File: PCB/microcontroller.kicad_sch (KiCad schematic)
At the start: 0 parts

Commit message: Further major components
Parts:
- added J1: Micro_SD_Card, Connector_Card:microSD_HC_Molex_47219-2001, symbol Connector:Micro_SD_Card
- added U2: STM32F401RETx, Package_QFP:LQFP-64_10x10mm_P0.5mm, symbol MCU_ST_STM32F4:STM32F401RETx
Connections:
- new net: U2.18 (VSS), U2.31 (VSS), U2.47 (VSS), U2.63 (VSS)
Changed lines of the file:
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@@
 (kicad_sch (version 20230121) (generator eeschema)
   (paper "A4")
+  (symbol (lib_id "Connector:Micro_SD_Card") (at 158.75 49.53 0) (unit 1)
+    (in_bom yes) (on_board yes) (dnp no) (fields_autoplaced)
+    (property "Reference" "J1" (at 159.385 31.75 0)
+      (effects (font (size 1.27 1.27)))
+    )
+    (property "Value" "Micro_SD_Card" (at 159.385 34.29 0)
+      (effects (font (size 1.27 1.27)))
+    )
+    (property "Footprint" "Connector_Card:microSD_HC_Molex_47219-2001" (at 187.96 41.91 0)
+      (effects (font (size 1.27 1.27)) hide)
+    )
+    (property "Datasheet" "http://katalog.we-online.de/em/datasheet/693072010801.pdf" (at 158.75 49.53 0)
+      (effects (font (size 1.27 1.27)) hide)
+    )
+    (pin "1")
+    (pin "2")
+    (pin "3")
+    (pin "4")
+    (pin "5")
+    (pin "6")
+    (pin "7")
+    (pin "8")
+    (pin "9")
+    (instances
+      (project "motor_tracker"
+        (path "/a8928dcf-7fea-46f0-8c15-a3fa49b43e6b/0c29d405-cd4c-45ef-9d08-777d8a682a5c"
+          (reference "J1") (unit 1)
+        )
+      )
+    )
+  )
+  (symbol (lib_id "MCU_ST_STM32F4:STM32F401RETx") (at 77.47 80.01 0) (unit 1)
+    (in_bom yes) (on_board yes) (dnp no) (fields_autoplaced)
+    (property "Reference" "U2" (at 81.9659 125.73 0)
+      (effects (font (size 1.27 1.27)) (justify left))
+    )
+    (property "Value" "STM32F401RETx" (at 81.9659 128.27 0)
+      (effects (font (size 1.27 1.27)) (justify left))
+    )
+    (property "Footprint" "Package_QFP:LQFP-64_10x10mm_P0.5mm" (at 64.77 123.19 0)
+      (effects (font (size 1.27 1.27)) (justify right) hide)
+    )
+    (property "Datasheet" "https://www.st.com/resource/en/datasheet/stm32f401re.pdf" (at 77.47 80.01 0)
+      (effects (font (size 1.27 1.27)) hide)
+    )
+    (pin "1")
+    (pin "10")
+    (pin "11")
+    (pin "12")
+    (pin "13")
+    (pin "14")
+    (pin "15")
+    (pin "16")
+    (pin "17")
+    (pin "18")
+    (pin "19")
+    (pin "2")
+    (pin "20")
+    (pin "21")
+    (pin "22")
+    (pin "23")
+    (pin "24")
+    (pin "25")
+    (pin "26")
+    (pin "27")
+    (pin "28")
+    (pin "29")
+    (pin "3")
+    (pin "30")
+    (pin "31")
+    (pin "32")
+    (pin "33")
+    (pin "34")
+    (pin "35")
+    (pin "36")
+    (pin "37")
+    (pin "38")
+    (pin "39")
+    (pin "4")
+    (pin "40")
+    (pin "41")
+    (pin "42")
+    (pin "43")
+    (pin "44")
+    (pin "45")
+    (pin "46")
+    (pin "47")
+    (pin "48")
+    (pin "49")
+    (pin "5")
+    (pin "50")
+    (pin "51")
+    (pin "52")
+    (pin "53")
+    (pin "54")
+    (pin "55")
+    (pin "56")
+    (pin "57")
+    (pin "58")
+    (pin "59")
+    (pin "6")
+    (pin "60")
+    (pin "61")
+    (pin "62")
+    (pin "63")
+    (pin "64")
+    (pin "7")
+    (pin "8")
+    (pin "9")
+    (instances
+      (project "motor_tracker"
+        (path "/a8928dcf-7fea-46f0-8c15-a3fa49b43e6b/0c29d405-cd4c-45ef-9d08-777d8a682a5c"
+          (reference "U2") (unit 1)
+        )
+      )
+    )
+  )
 )

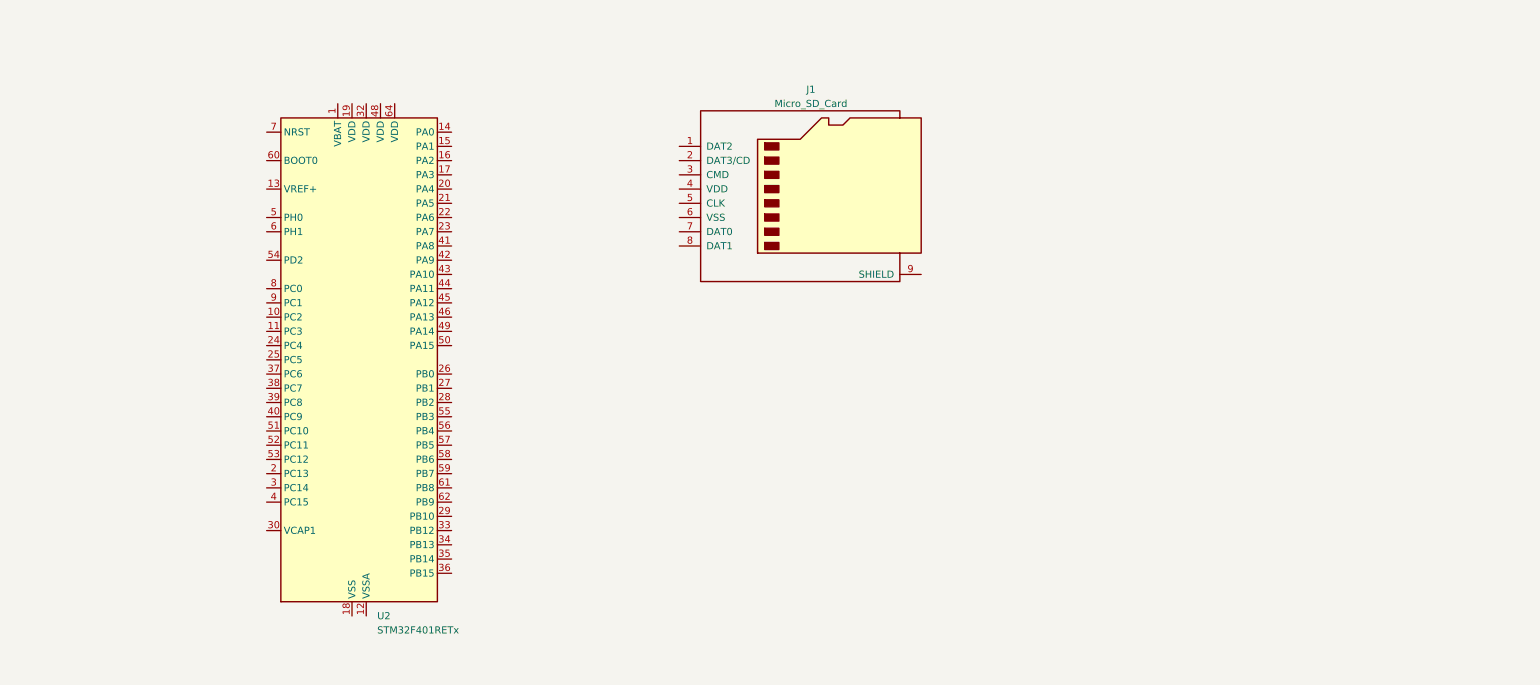
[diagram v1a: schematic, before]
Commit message: Added basic componenets to uC
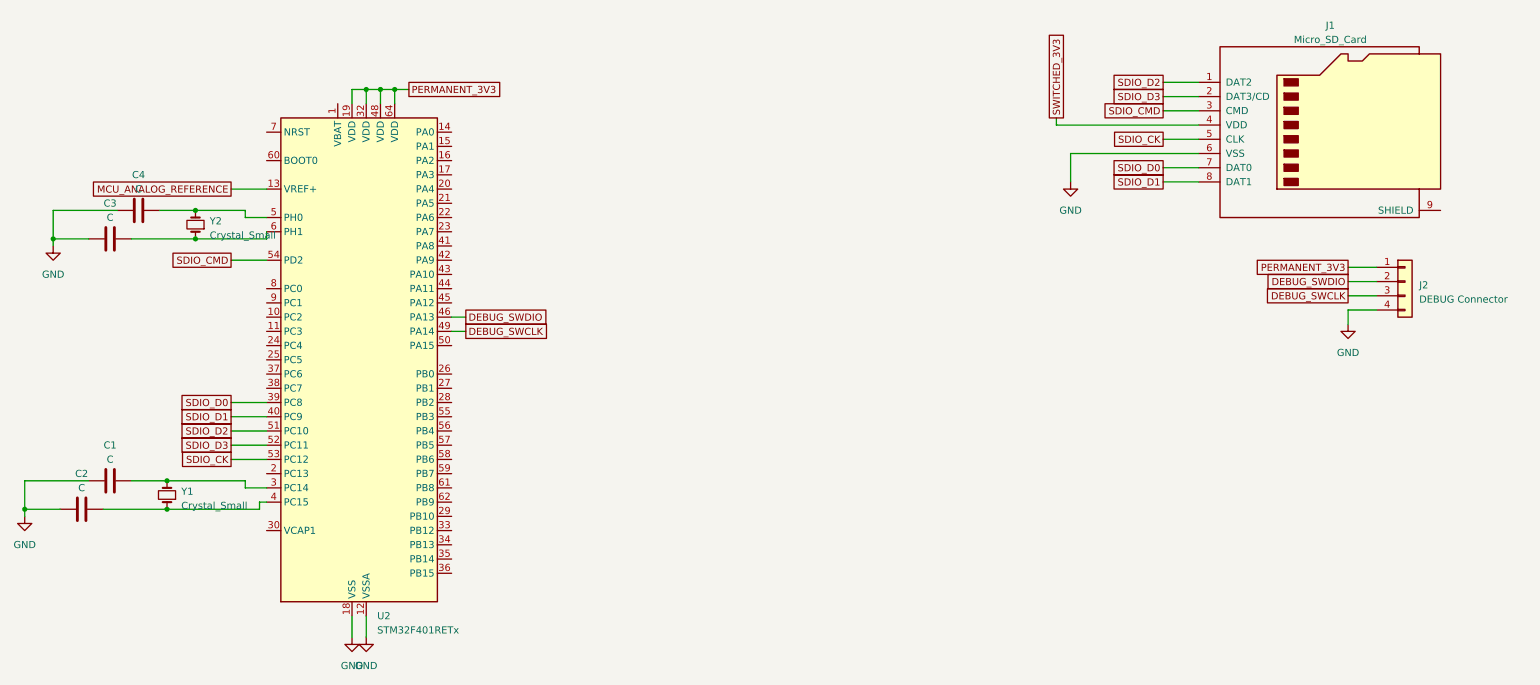
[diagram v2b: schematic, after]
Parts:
- added C1, C2, C3, C4: C, Capacitor_SMD:C_0201_0603Metric_Pad0.64x0.40mm_HandSolder, symbol Device:C
- added J2: DEBUG Connector, Connector_PinHeader_2.54mm:PinHeader_1x04_P2.54mm_Vertical, symbol Connector_Generic:Conn_01x04
- added Y1: Crystal_Small, Crystal:Crystal_SMD_5032-4Pin_5.0x3.2mm, symbol Device:Crystal_Small
- added Y2: Crystal_Small, Crystal:Crystal_C38-LF_D3.0mm_L8.0mm_Horizontal_1EP_style1, symbol Device:Crystal_Small
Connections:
- net SDIO_D2: now reaches J1.1 (DAT2)
- net SDIO_D2: now also U2.51 (PC10)
- net SDIO_D3: now reaches J1.2 (DAT3/CD)
- net SDIO_D3: now also U2.52 (PC11)
- net SDIO_CMD: now reaches J1.3 (CMD)
- net SDIO_CMD: now also U2.54 (PD2)
- net SWITCHED_3V3: now reaches J1.4 (VDD)
- net SDIO_CK: now reaches J1.5 (CLK)
- net SDIO_CK: now also U2.53 (PC12)
- net GND: now reaches J1.6 (VSS)
- net GND: now also U2.12 (VSSA), U2.18 (VSS), U2.31 (VSS), U2.47 (VSS), U2.63 (VSS), C1.2, C2.2, C3.2, C4.2, J2.4 (Pin_4)
- net SDIO_D0: now reaches J1.7 (DAT0)
- net SDIO_D0: now also U2.39 (PC8)
- net SDIO_D1: now reaches J1.8 (DAT1)
- net SDIO_D1: now also U2.40 (PC9)
- net MCU_ANALOG_REFERENCE: now reaches U2.13 (VREF+)
- net PERMANENT_3V3: now reaches U2.19 (VDD)
- net PERMANENT_3V3: now also U2.32 (VDD), U2.48 (VDD), U2.64 (VDD), J2.1 (Pin_1)
- net at U2.3 (PC14): now also C1.1, Y1.2
- net at U2.4 (PC15): now also C2.1, Y1.1
- net DEBUG_SWDIO: now reaches U2.46 (PA13)
- net DEBUG_SWDIO: now also J2.2 (Pin_2)
- net DEBUG_SWCLK: now reaches U2.49 (PA14)
- net DEBUG_SWCLK: now also J2.3 (Pin_3)
- net at U2.5 (PH0): now also C4.1, Y2.2
- net at U2.6 (PH1): now also C3.1, Y2.1
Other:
- moved on the sheet: J1

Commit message: Added USB connector
Added acceleration sensor

Added combined gyro and acceleration sensor
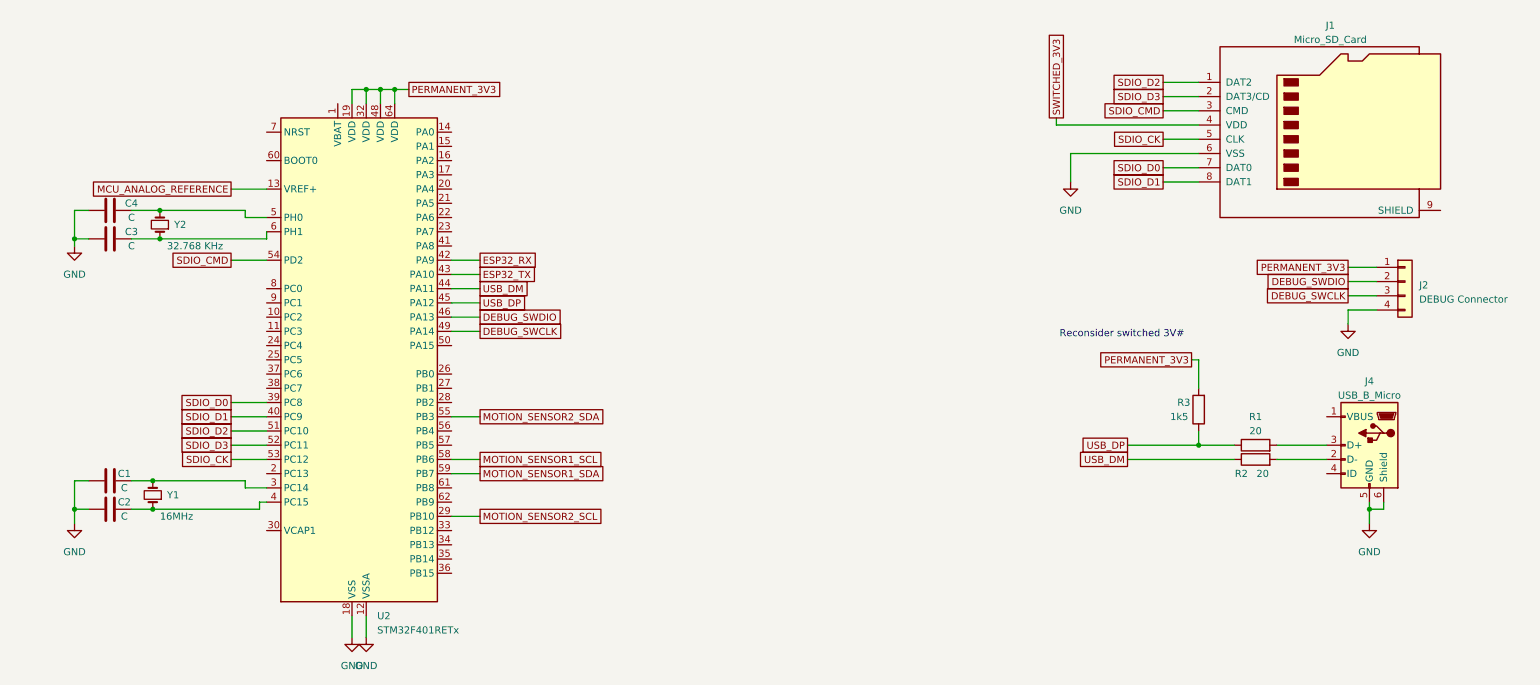
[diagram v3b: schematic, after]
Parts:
- added J4: USB_B_Micro, Connector_USB:USB_Micro-B_Molex-105017-0001, symbol Connector:USB_B_Micro
- added R1, R2: 20, Resistor_SMD:R_0603_1608Metric_Pad0.98x0.95mm_HandSolder, symbol Device:R
- added R3: 1k5, Resistor_SMD:R_0603_1608Metric_Pad0.98x0.95mm_HandSolder, symbol Device:R
- J1: Hestore (none) -> https://www.hestore.hu/prod_10035282.html
- Y1: value Crystal_Small -> 16MHz
- Y2: value Crystal_Small -> 32.768 KHz
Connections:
- net GND: now also J4.5 (GND), J4.6 (Shield)
- net PERMANENT_3V3: now also R3.2
- net MOTION_SENSOR2_SCL: now reaches U2.29 (PB10)
- net ESP32_RX: now reaches U2.42 (PA9)
- net ESP32_TX: now reaches U2.43 (PA10)
- net USB_DM: now reaches U2.44 (PA11)
- net USB_DM: now also R2.1
- net USB_DP: now reaches U2.45 (PA12)
- net USB_DP: now also R1.1, R3.1
- net MOTION_SENSOR2_SDA: now reaches U2.55 (PB3)
- net MOTION_SENSOR1_SCL: now reaches U2.58 (PB6)
- net MOTION_SENSOR1_SDA: now reaches U2.59 (PB7)
- new net: J4.2 (D-), R2.2
- new net: J4.3 (D+), R1.2
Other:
- note added: "Reconsider switched 3V#"
- moved on the sheet: C2, C4, Y1, Y2

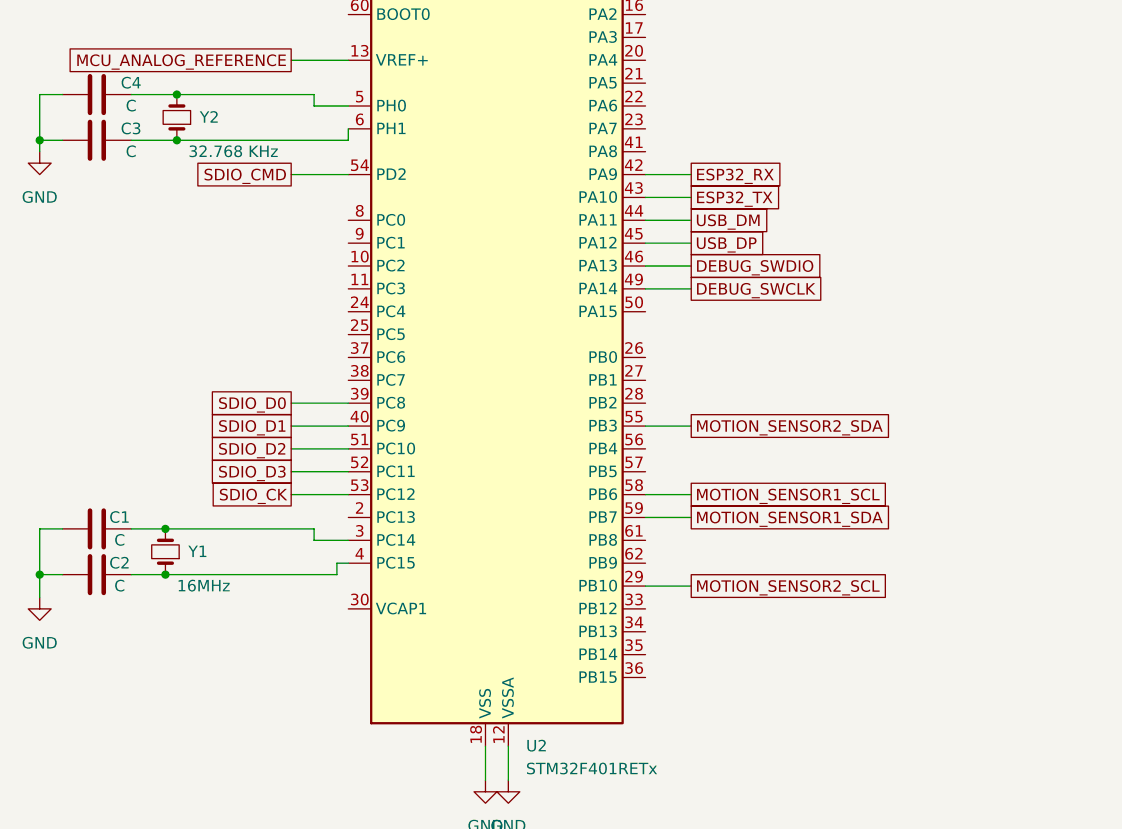
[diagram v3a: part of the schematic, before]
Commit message: Added connector for GPS
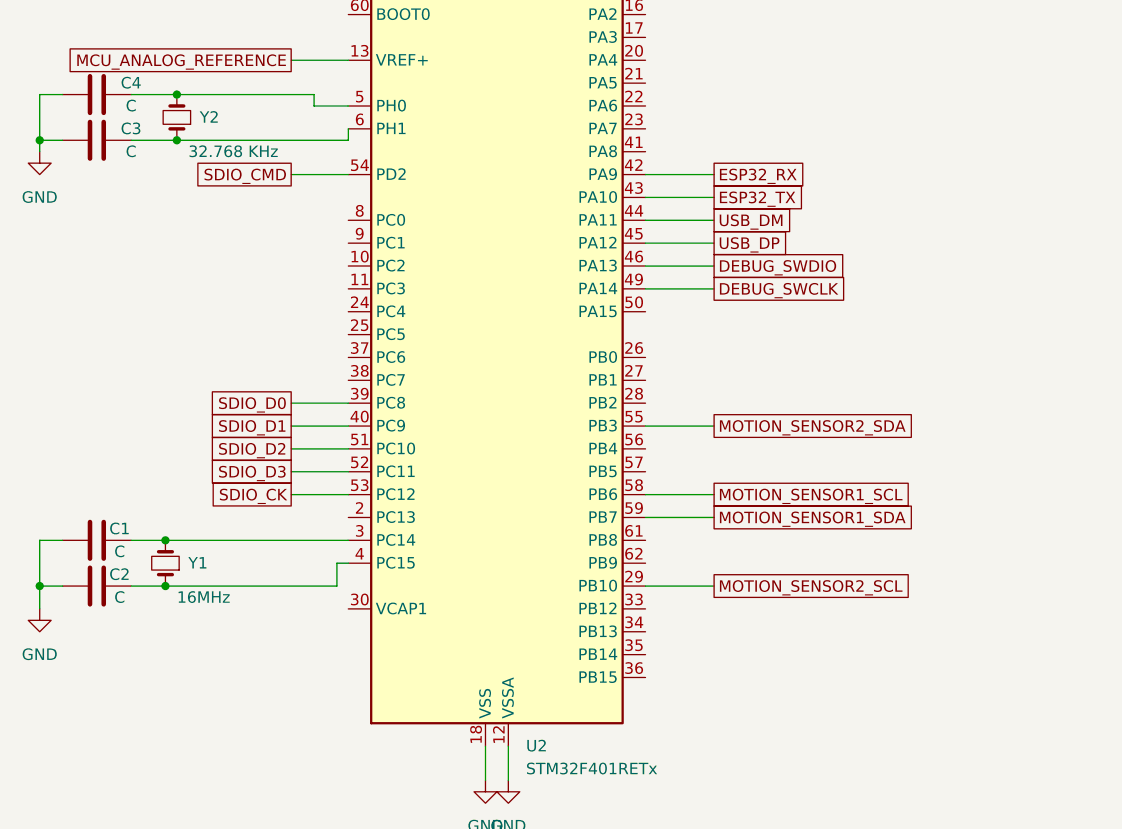
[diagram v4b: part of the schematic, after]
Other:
- moved on the sheet: C1, C2, Y1

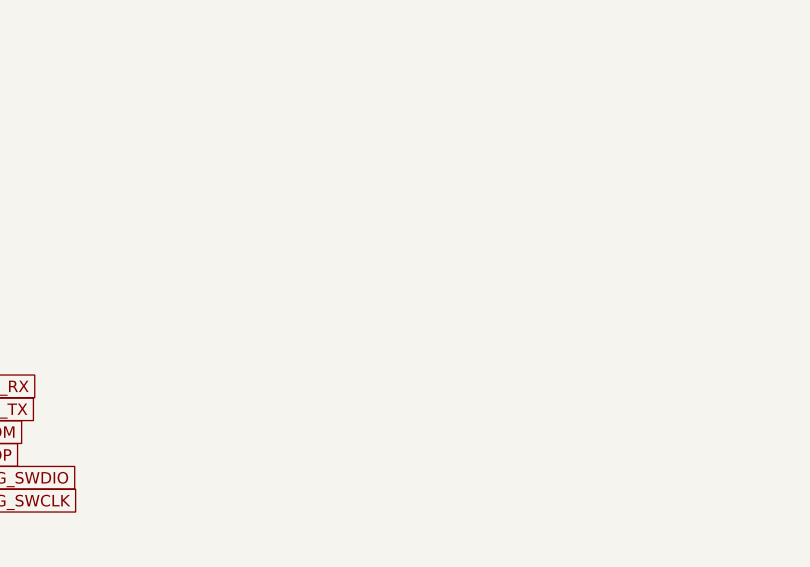
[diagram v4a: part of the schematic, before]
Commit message: Polarity protection in Power Management
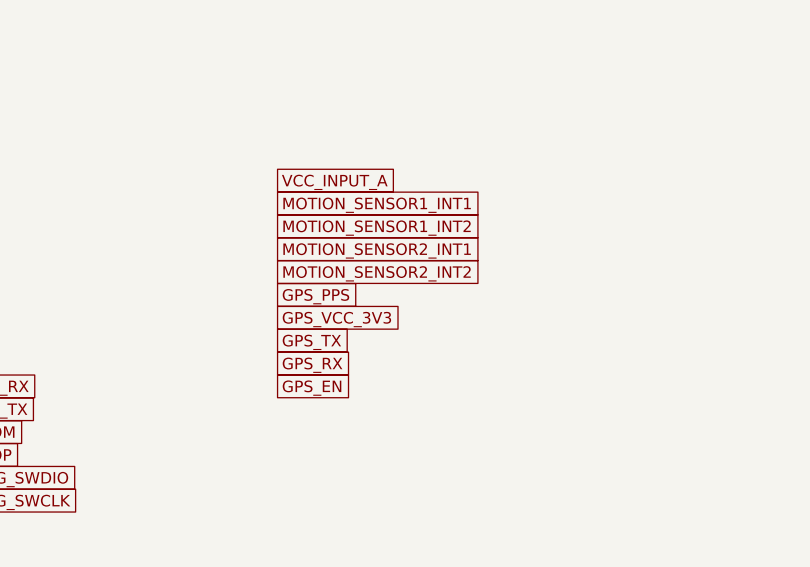
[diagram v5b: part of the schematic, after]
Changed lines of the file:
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@@
     (effects (font (size 1.27 1.27)) (justify right bottom))
   )
+  (global_label "MOTION_SENSOR1_INT1" (shape passive) (at 139.7 41.91 0) (fields_autoplaced)
+    (effects (font (size 1.27 1.27)) (justify left))
+    (property "Intersheetrefs" "${INTERSHEET_REFS}" (at 163.2659 41.91 0)
+      (effects (font (size 1.27 1.27)) (justify left) hide)
+    )
+  )
   (global_label "SDIO_D1" (shape passive) (at 222.25 48.26 180) (fields_autoplaced)
     (effects (font (size 1.27 1.27)) (justify right))
@@
     )
   )
+  (global_label "MOTION_SENSOR2_INT1" (shape passive) (at 139.7 46.99 0) (fields_autoplaced)
+    (effects (font (size 1.27 1.27)) (justify left))
+    (property "Intersheetrefs" "${INTERSHEET_REFS}" (at 163.2659 46.99 0)
+      (effects (font (size 1.27 1.27)) (justify left) hide)
+    )
+  )
+  (global_label "GPS_EN" (shape passive) (at 139.7 62.23 0) (fields_autoplaced)
+    (effects (font (size 1.27 1.27)) (justify left))
+    (property "Intersheetrefs" "${INTERSHEET_REFS}" (at 148.6911 62.23 0)
+      (effects (font (size 1.27 1.27)) (justify left) hide)
+    )
+  )
   (global_label "SDIO_CMD" (shape passive) (at 222.25 35.56 180) (fields_autoplaced)
     (effects (font (size 1.27 1.27)) (justify right))
@@
     )
   )
+  (global_label "VCC_INPUT_A" (shape passive) (at 139.7 39.37 0) (fields_autoplaced)
+    (effects (font (size 1.27 1.27)) (justify left))
+    (property "Intersheetrefs" "${INTERSHEET_REFS}" (at 153.6503 39.37 0)
+      (effects (font (size 1.27 1.27)) (justify left) hide)
+    )
+  )
+  (global_label "GPS_VCC_3V3" (shape passive) (at 139.7 54.61 0) (fields_autoplaced)
+    (effects (font (size 1.27 1.27)) (justify left))
+    (property "Intersheetrefs" "${INTERSHEET_REFS}" (at 154.3154 54.61 0)
+      (effects (font (size 1.27 1.27)) (justify left) hide)
+    )
+  )
+  (global_label "GPS_TX" (shape passive) (at 139.7 57.15 0) (fields_autoplaced)
+    (effects (font (size 1.27 1.27)) (justify left))
+    (property "Intersheetrefs" "${INTERSHEET_REFS}" (at 148.3887 57.15 0)
+      (effects (font (size 1.27 1.27)) (justify left) hide)
+    )
+  )
   (global_label "USB_DM" (shape passive) (at 102.87 67.31 0) (fields_autoplaced)
     (effects (font (size 1.27 1.27)) (justify left))
@@
     )
   )
+  (global_label "GPS_RX" (shape passive) (at 139.7 59.69 0) (fields_autoplaced)
+    (effects (font (size 1.27 1.27)) (justify left))
+    (property "Intersheetrefs" "${INTERSHEET_REFS}" (at 148.6911 59.69 0)
+      (effects (font (size 1.27 1.27)) (justify left) hide)
+    )
+  )
   (global_label "SDIO_D2" (shape passive) (at 55.88 92.71 180) (fields_autoplaced)
     (effects (font (size 1.27 1.27)) (justify right))
@@
     )
   )
+  (global_label "GPS_PPS" (shape passive) (at 139.7 52.07 0) (fields_autoplaced)
+    (effects (font (size 1.27 1.27)) (justify left))
+    (property "Intersheetrefs" "${INTERSHEET_REFS}" (at 149.9611 52.07 0)
+      (effects (font (size 1.27 1.27)) (justify left) hide)
+    )
+  )
   (global_label "DEBUG_SWDIO" (shape passive) (at 102.87 72.39 0) (fields_autoplaced)
     (effects (font (size 1.27 1.27)) (justify left))
@@
     )
   )
+  (global_label "MOTION_SENSOR2_INT2" (shape passive) (at 139.7 49.53 0) (fields_autoplaced)
+    (effects (font (size 1.27 1.27)) (justify left))
+    (property "Intersheetrefs" "${INTERSHEET_REFS}" (at 163.2659 49.53 0)
+      (effects (font (size 1.27 1.27)) (justify left) hide)
+    )
+  )
   (global_label "USB_DM" (shape passive) (at 215.9 97.79 180) (fields_autoplaced)
     (effects (font (size 1.27 1.27)) (justify right))
@@
     )
   )
+  (global_label "MOTION_SENSOR1_INT2" (shape passive) (at 139.7 44.45 0) (fields_autoplaced)
+    (effects (font (size 1.27 1.27)) (justify left))
+    (property "Intersheetrefs" "${INTERSHEET_REFS}" (at 163.2659 44.45 0)
+      (effects (font (size 1.27 1.27)) (justify left) hide)
+    )
+  )
